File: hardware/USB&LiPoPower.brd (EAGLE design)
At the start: 47 x 40.5 mm, 48 parts, among them Q1 IRLML5203, Q2 IRLML5203, U2 ACS711ELCTR-12AB-T, U3 ACS711ELCTR-12AB-T, U4 I-02247_NJM2845, U5 CH004-2032LF

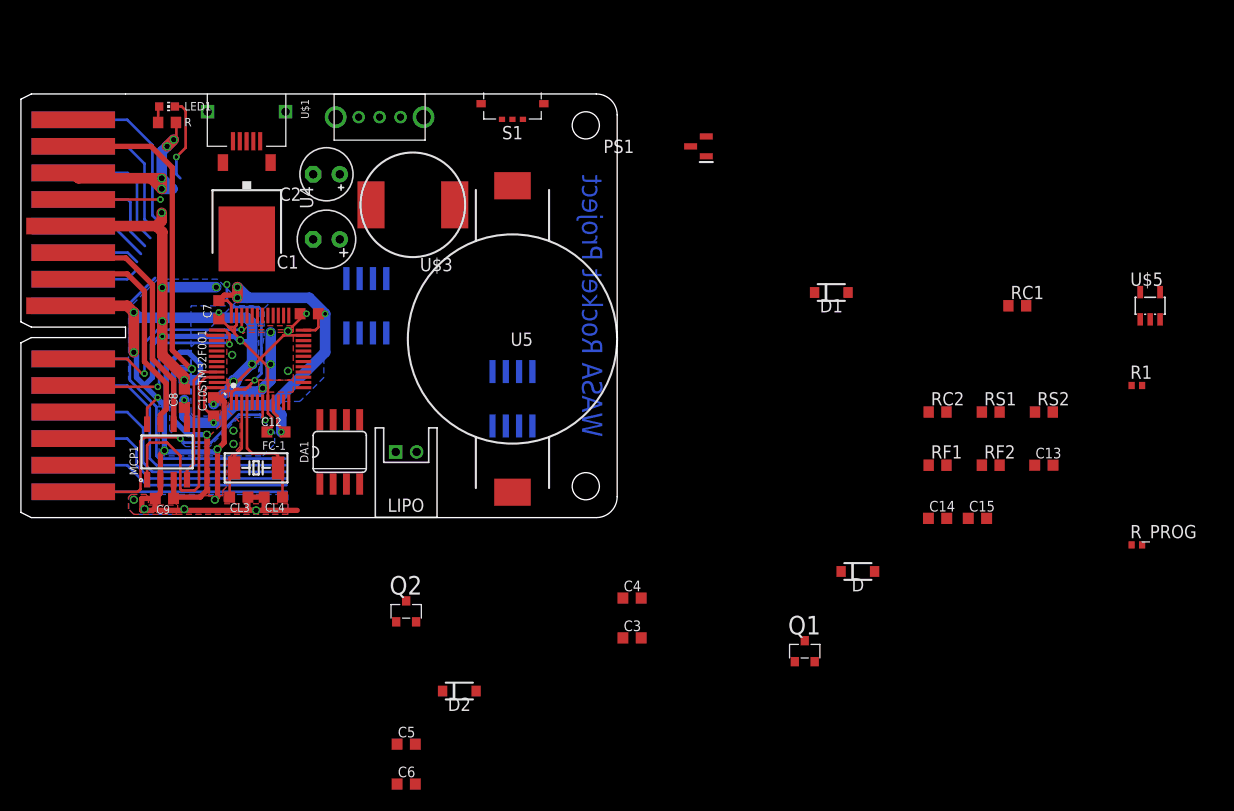
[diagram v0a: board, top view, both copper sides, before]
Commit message: Layout USB and LiPo power board
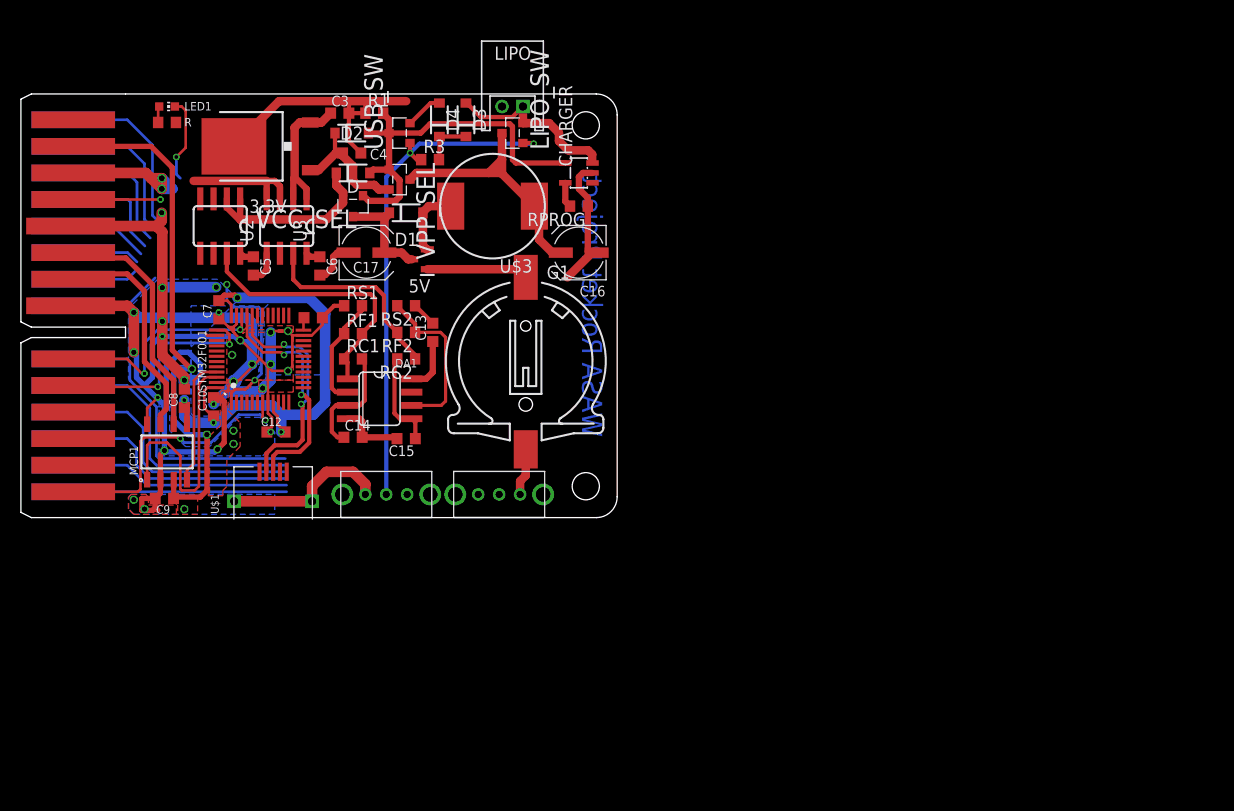
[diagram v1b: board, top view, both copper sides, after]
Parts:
- removed C1: 47µF, rcl:E2,5-6
- removed C2: 22µF, rcl:E2,5-5
- removed CL3, CL4: 15pF, rcl:C0603K
- removed FC-1: 32.768kHz, crystal':FC-255
- removed PS1: HT7750A_SOT23-3, HT7750A_SOT23-3:SOT95P190X145-3N
- removed Q1, Q2: IRLML5203, transistor-power:MICRO3
- removed R_PROG: (no value), rcl:R0402
- removed S1: SSAJ120100, SSAJ120100:SSAJ120100
- removed U$5: MCP73831, mcp73831:SOT23-5L
- removed U$6: SK-12D01-VG4, switches:SK-12D01-VG4
- removed U4: I-02247_NJM2845, akizuki:TO252
- removed U5: CH004-2032LF, CH004-2032LF:CH004-2032LF
- added 3.3V: I-02247_NJM2845, akizuki:TO252
- added 5V: HT7750A_SOT23-3, HT7750A_SOT23-3:SOT95P190X145-3N
- added BACKUP, POWER: SK-12D01-VG4, switches:SK-12D01-VG4
- added C16, C17: 47µF, rcl:UD-5X5,8_NICHICON
- added CHARGER: MCP73831, mcp73831:SOT23-5L
- added D3, D4: RB160M-30TR, RB160M-30TR:SODFL3516X90N
- added G1: CH291-1220LF, battery:CH291-1220LF
- added LIPO_SW, USB_SW, VCC_SEL, VPP_SEL: IRLML5203, transistor-power:MICRO3
- added R3: 100k, rcl:R0603
- added RPROG: (no value), rcl:R0603
- R1: device rcl:R0402 -> rcl:R0603
- moved R1 77.4 mm to (33.8, 18.4)
- moved RC1 63.7 mm to (31.8, -5.08)
- moved RS2 61.8 mm to (36.8, 0.00), turned to 180 degrees
- moved RS1 61.8 mm to (31.8, 0.00)
- moved D 61.5 mm to (31.8, 12.7)
- moved C13 59.8 mm to (39.4, -2.54), turned to 90 degrees
- moved C3 57.4 mm to (30.5, 18.4)
- moved RF2 57.3 mm to (36.8, -2.54), turned to 180 degrees
- moved RF1 57.3 mm to (31.8, -2.67)
- moved C14 56.4 mm to (31.8, -12.6)
- moved C15 55.1 mm to (36.8, -12.7), turned to 180 degrees
- moved D2 54.3 mm to (31.6, 16.5)
- moved RC2 51.1 mm to (36.8, -5.08), turned to 180 degrees
- moved C4 50.3 mm to (31.6, 14.6)
- moved C6 50.2 mm to (28.6, 3.81), turned to 270 degrees
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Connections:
- net N$3 renamed 5VC_OUT
- net N$4 renamed 3.3VC_OUT
- removed net BU+: S1.1, U5.2
- removed net N$2: D1.2, PS1.2, U$3.2
- removed net N$71: CL4.2, FC-1.1, STM32F001.4
- removed net N$72: CL3.2, FC-1.2, STM32F001.3
- removed net VCC'1: C4.1, D2.1, Q2.2, U4.1
- new net BAT+: BACKUP.B, G1.+
- new net N$10: D3.1, D4.1, R3.2
- new net N$9: LIPO_SW.1, POWER.C, R3.1, USB_SW.1
- new net USB_5V: D4.2, U$1.1, USB_SW.2
- new net VBU: BACKUP.C, U$2.4
- new net VCCG_IN: 5V.2, D1.2, U$3.2
- net 3.3V: now also 3.3V.3; no longer U4.3
- net 5V: now also VCC_SEL.2; no longer Q1.2
- net GND: now also 3.3V.2, 5V.1, C16.-, C17.-, CHARGER.2, G1.-, POWER.A, RPROG.1; no longer C1.-, C2.-, CL3.1, CL4.1, PS1.1, R_PROG.2, U$5.2, U4.2, U5.1
- net LIPO+: now also CHARGER.3, D3.2, LIPO_SW.2; no longer U$5.3, U$6.C
- net N$1: now also CHARGER.5, RPROG.2; no longer R_PROG.1, U$5.5
- net VBAT: no longer S1.C, U$2.4
- net VCC_GEN: now also 5V.3, C17.+, VCC_SEL.3; no longer C2.+, PS1.3, Q1.3
- net VCC_USB: now also CHARGER.4, USB_SW.3, VCC_SEL.1, VPP_SEL.1; no longer Q1.1, Q2.1, U$1.1, U$5.4
- net VLIPO: now also C16.+, LIPO_SW.3, VPP_SEL.3; no longer C1.+, Q2.3, U$6.B
- net VPP: now also 3.3V.1, C4.1, D2.1, VPP_SEL.2
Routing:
- net GND: track 192.6 -> 256.1 mm, vias 31 -> 28
- net N$9: track 0.00 -> 49.2 mm, vias 0 -> 2
- net VCC_USB: track 0.00 -> 37.1 mm
- net 5VC: track 0.00 -> 26.0 mm
- net VLIPO: track 0.00 -> 25.1 mm
- net USB_D+: track 0.00 -> 22.6 mm, vias 0 -> 2
- net USB_D-: track 0.00 -> 22.4 mm, vias 0 -> 2
- net 3.3VC: track 0.00 -> 19.1 mm
- net 5V: track 0.00 -> 18.3 mm
- net LIPO+: track 0.00 -> 17.0 mm
- net N$6: track 0.00 -> 15.9 mm
- net 3.3V: track 0.00 -> 13.5 mm
- net VPP: track 0.00 -> 12.6 mm
- net N$71: track 11.8 -> 0.00 mm
- net 5VC_OUT: track 0.00 -> 11.1 mm
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
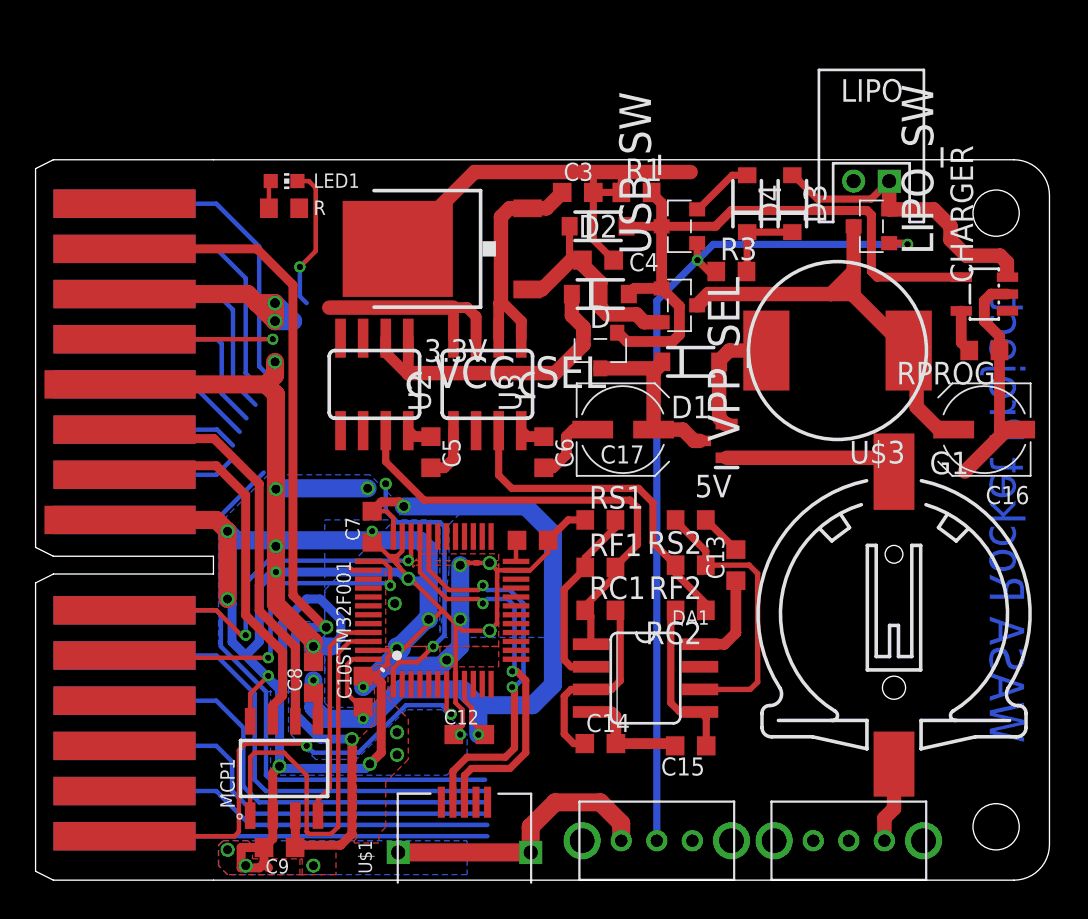
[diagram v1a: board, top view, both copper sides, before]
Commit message: Complete USB & LiPo power board
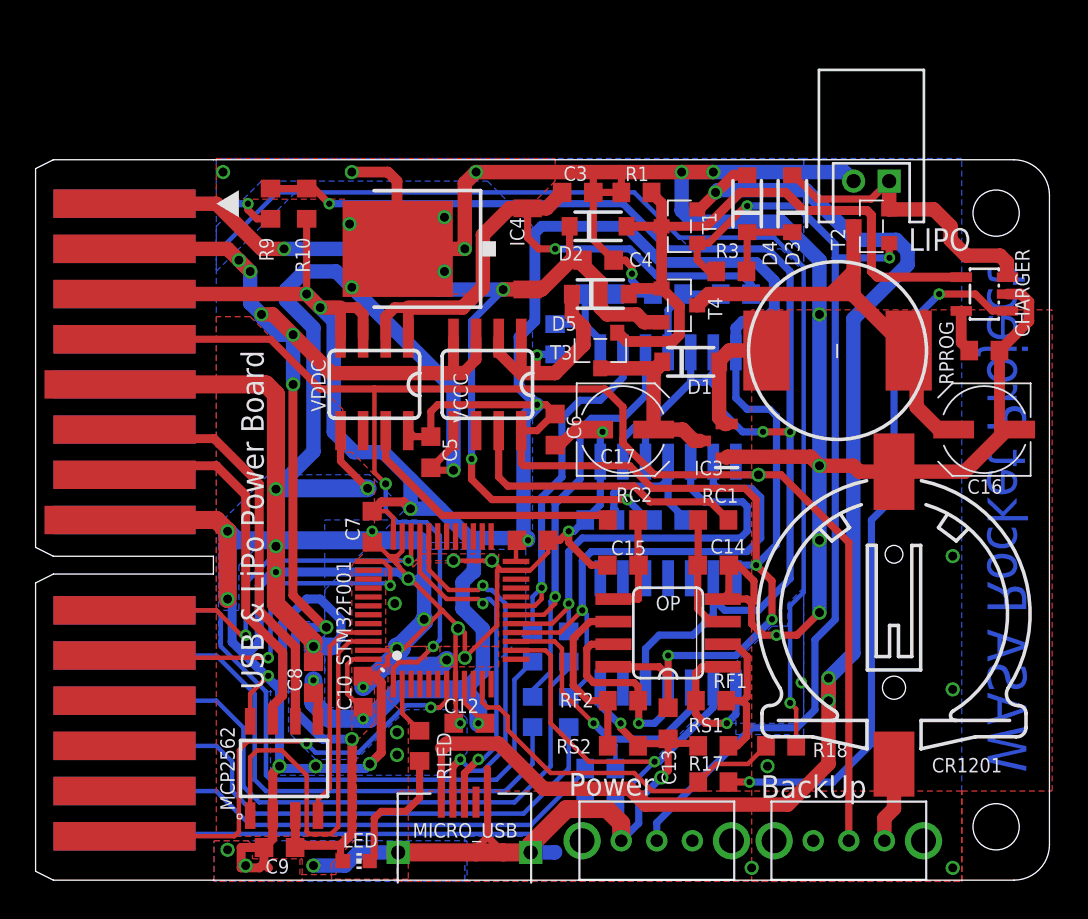
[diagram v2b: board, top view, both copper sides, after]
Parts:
- removed DA1: NJM2904M, ic-jrc:SO-8
- removed LED1: (no value), led:CHIP-LED0603
- removed R: 1K, rcl:R0603
- added IC1, IC2: 4066D, 40xx:SO14
- added LED: (no value), led:CHIP-LED0603
- added OP: NJM2904M, ic-jrc:SO-8
- added R10, R17: 10k, resistor:R0603
- added R11, R12, R13, R14, R15, R16, R18, R9: 1k, resistor:R0603
- added R2, R5, R6, R7, R8: 10k, rcl:R0603
- added R4: 1k, rcl:R0603
- added RLED: 1K, rcl:R0603
- C10, C11, C12, C5, C6, C7, C8, C9: value (none) -> 0.1µF
- moved RS1 14.2 mm to (38.1, -12.7)
- moved RS2 13.3 mm to (33.0, -12.7)
- moved C14 11.9 mm to (38.1, -2.54)
- moved C15 10.9 mm to (33.0, -2.54)
- moved RF1 9.74 mm to (38.0, -10.2), turned to 180 degrees
- moved C13 9.67 mm to (35.6, -11.4), turned to 270 degrees
- moved RF2 8.52 mm to (33.0, -10.2), turned to 0 degrees
- moved RC1 8.13 mm to (38.1, 0.00), turned to 180 degrees
- moved RC2 6.35 mm to (33.0, 0.00), turned to 0 degrees
- moved C6 1.42 mm to (29.2, 5.08)
- moved C12 0.63 mm to (24.4, -11.4)
- renumbered 3.3V to IC4, 5V to IC3, D to D5, G1 to CR1201, LIPO_SW to T2, MCP1 to MCP2562, U$1 to MICRO_USB, U$3 to I, U2 to VDDC, U3 to VCCC, USB_SW to T1, VCC_SEL to T3, VPP_SEL to T4
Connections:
- removed net N$45: U$2.23
- removed net N$46: U$2.22
- removed net N$47: U$2.21
- removed net N$48: U$2.20
- removed net N$49: U$2.19
- removed net N$50: U$2.18
- removed net N$51: STM32F001.10
- removed net N$52: STM32F001.11
- removed net N$53: STM32F001.12
- removed net N$54: STM32F001.13
- removed net N$55: STM32F001.14
- removed net N$56: STM32F001.15
- removed net N$57: STM32F001.16
- removed net N$58: STM32F001.17
- removed net N$59: STM32F001.29
- removed net N$62: STM32F001.18
- removed net N$63: STM32F001.19
- removed net N$64: STM32F001.20
- removed net N$65: STM32F001.21
- removed net N$66: STM32F001.22
- removed net N$67: STM32F001.25
- removed net N$68: STM32F001.26
- removed net N$69: STM32F001.27
- removed net N$70: STM32F001.28
- removed net N$76: LED1.A, R.2
- removed net VBAT: STM32F001.1
- new net !HIL!: IC1.13, IC1.5, IC2.12, IC2.13, IC2.5, IC2.6, R10.1, R9.1
- new net 3.3VC': IC1.4, OP.7, RF2.2
- new net 3.3VC_OUT': RC2.1, VDDC.7
- new net 5VC': IC1.1, OP.1, RF1.2
- new net 5VC_OUT': RC1.1, VCCC.7
- new net N$2: CHARGER.1, R17.2
- new net N$3: LED.C, RLED.1
- new net PVCC: IC2.8, R5.1, R6.2
- new net PVDD: IC2.11, R7.1, R8.2
- new net PVPP: IC2.4, R2.1, R4.2
- new net STAT: R17.1, R18.1, STM32F001.11
- new net SVBU: IC2.2, R14.1, STM32F001.16
- new net SVCC: IC2.9, R11.1, STM32F001.19
- new net SVDD: IC2.10, R12.1, STM32F001.18
- new net SVPP: IC2.3, R13.1, STM32F001.17
- net 3.3V: now also R7.2, VDDC.1, VDDC.2; no longer VCCC.1, VCCC.2
- net 3.3VC: now also IC1.3, R15.1, STM32F001.15; no longer DA1.7, RC2.1, RF2.2, VCCC.7
- net 3.3VC_OUT: now also OP.5; no longer DA1.5
- net 5V: now also R5.2, VCCC.1, VCCC.2; no longer VDDC.1, VDDC.2
- net 5VC: now also IC1.2, R16.1, STM32F001.14; no longer DA1.1, RC1.1, RF1.2, VDDC.7
- net 5VC_OUT: now also OP.3; no longer DA1.3
- net GND: now also IC1.7, IC2.7, OP.4, R4.1, R6.1, R8.1; no longer DA1.4
- net N$33: now also R16.2
- net N$34: now also R15.2
- net N$35: now also R14.2
- net N$36: now also R13.2
- net N$43: now also R12.2
- net N$44: now also R11.2
- net N$5: now also OP.2; no longer DA1.2
- net N$6: now also OP.6; no longer DA1.6
- net N$73: now also RLED.2, STM32F001.2; no longer LED1.C, STM32F001.38
- net N$74: now also R9.2
- net N$75: now also R18.2
- net VBU: now also IC2.1, STM32F001.1
- net VCC: now also LED.A, VCCC.3, VCCC.4; no longer VDDC.3, VDDC.4
- net VDD: now also IC1.14, IC2.14, OP.8, R10.2, VDDC.3, VDDC.4; no longer DA1.8, R.1, VCCC.3, VCCC.4
- net VPP: now also R2.2
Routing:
- net GND: track 256.1 -> 391.9 mm, vias 28 -> 55
- net VDD: track 86.6 -> 189.5 mm, vias 6 -> 11
- net !HIL!: track 0.00 -> 82.9 mm, vias 0 -> 3
- net VBU: track 8.34 -> 86.2 mm, vias 1 -> 3
- net USB_5V: track 3.61 -> 76.4 mm, vias 0 -> 3
- net N$75: track 14.3 -> 68.6 mm, vias 0 -> 1
- net VPP: track 12.6 -> 59.8 mm, vias 0 -> 4
- net N$2: track 0.00 -> 40.0 mm, vias 0 -> 2
- net SVBU: track 0.00 -> 29.5 mm, vias 0 -> 1
- net SVDD: track 0.00 -> 25.9 mm, vias 0 -> 1
- net SVPP: track 0.00 -> 25.0 mm, vias 0 -> 1
- net VCC: track 51.1 -> 72.3 mm, vias 2 -> 7
- net SVCC: track 0.00 -> 20.7 mm, vias 0 -> 1
- net STAT: track 0.00 -> 20.5 mm
- net 3.3V: track 13.5 -> 33.3 mm, vias 0 -> 1
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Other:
- board text added: "BackUp"
- board text added: "Power"
- board text added: "USB & LiPo Power Board"
